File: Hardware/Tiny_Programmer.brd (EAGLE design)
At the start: 59.7 x 15.2 mm, 31 parts, among them Q1 16MHz, U1 ATTINY84, X1 USB-A-H

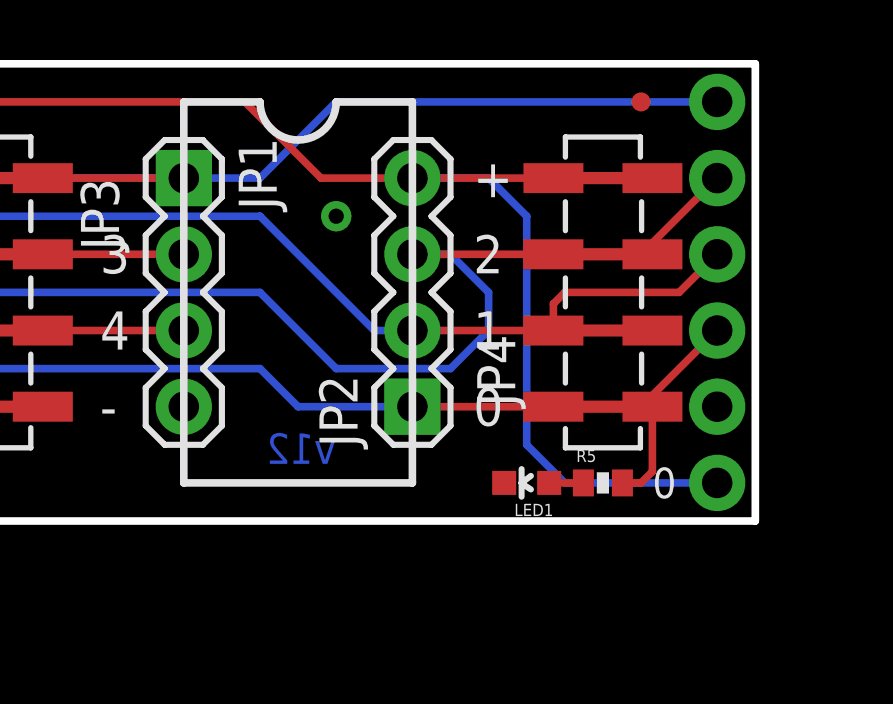
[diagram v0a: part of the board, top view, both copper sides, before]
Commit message: Modifies the new 6-pin SIP to be more compatible with an FTDI.
The new pin out should allow MOSI and MISO to bit-bang serial and
communicate over an FTDI connection for serial debuggin.
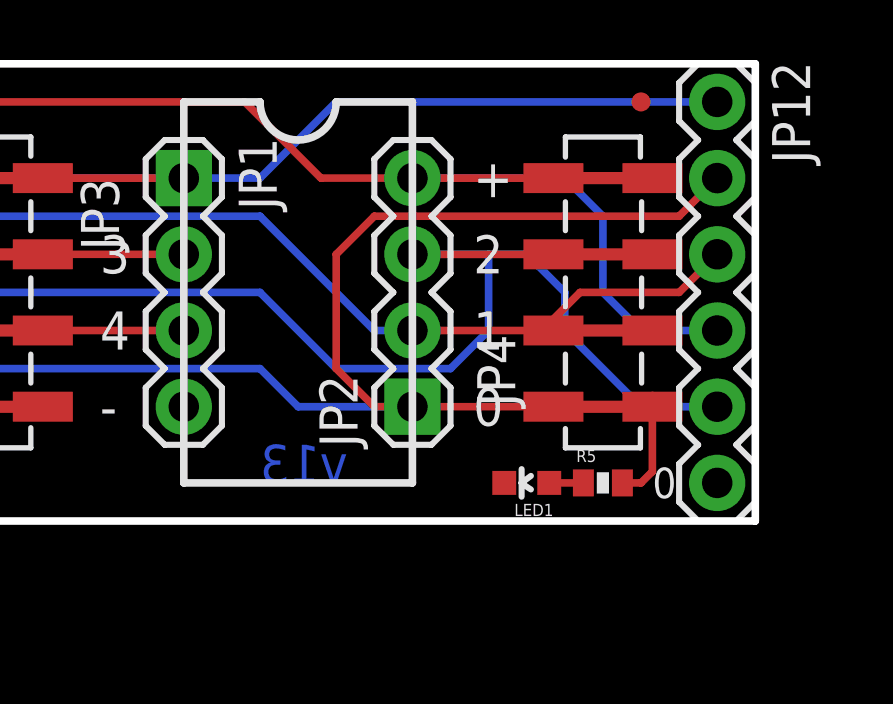
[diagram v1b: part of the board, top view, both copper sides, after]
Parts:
- flipped JP12 to the top
- renumbered JP10 to JP12
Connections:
- net GND: now also JP12.6; no longer JP12.5
- net MOSI: now also JP12.2; no longer JP12.4
- net SCK: now also JP12.5; no longer JP12.2
- net VCC: now also JP12.4; no longer JP12.6
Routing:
- net MOSI: track 64.9 -> 82.5 mm
- net SCK: track 58.0 -> 65.8 mm
- net VCC: track 86.5 -> 81.5 mm
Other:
- board text added: "GND"
- board text added: "v13"
- board text removed: "v12"
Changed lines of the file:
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@@
 <?xml version="1.0" encoding="utf-8"?>
 <!DOCTYPE eagle SYSTEM "eagle.dtd">
-<eagle version="6.4">
+<eagle version="6.5.0">
 <drawing>
 <settings>
@@
 <layer number="106" name="bPlate" color="7" fill="1" visible="no" active="yes"/>
 <layer number="107" name="Crop" color="7" fill="1" visible="no" active="yes"/>
+<layer number="108" name="tplace-old" color="10" fill="1" visible="yes" active="yes"/>
+<layer number="109" name="ref-old" color="11" fill="1" visible="yes" active="yes"/>
 <layer number="116" name="Patch_BOT" color="9" fill="4" visible="no" active="yes"/>
 <layer number="121" name="_tsilk" color="7" fill="1" visible="no" active="yes"/>
@@
 <wire x1="43.18" y1="13.97" x2="45.72" y2="13.97" width="0.254" layer="21" curve="180"/>
 <text x="38.1" y="1.27" size="1.778" layer="22" font="vector" ratio="15" rot="MR0">Tiny Programmer</text>
-<text x="45.72" y="1.905" size="1.016" layer="16" font="vector" ratio="20" rot="MR0">v12</text>
+<text x="46.101" y="1.27" size="1.27" layer="16" font="vector" ratio="20" rot="MR0">v13</text>
 <text x="1.27" y="-12.7" size="1.778" layer="27" font="vector" ratio="15">David A. Mellis, Jordan McConnell</text>
 <text x="23.241" y="13.97" size="0.8128" layer="21" font="vector" ratio="15" rot="SR0">RST</text>
@@
 <wire x1="0.889" y1="2.159" x2="1.016" y2="2.286" width="0.254" layer="49"/>
 <text x="55.499" y="6.731" size="0.8128" layer="22" font="vector" ratio="15" rot="SMR90">ISP</text>
-<text x="55.88" y="0.254" size="0.8128" layer="22" font="vector" ratio="15" rot="SMR90">VCC</text>
+<text x="55.88" y="0.254" size="0.8128" layer="22" font="vector" ratio="15" rot="SMR90">GND</text>
 <text x="55.88" y="12.954" size="0.8128" layer="22" font="vector" ratio="15" rot="SMR90">RST</text>
 <wire x1="55.88" y1="8.89" x2="55.88" y2="12.192" width="0.254" layer="22"/>
@@
 <element name="JP7" library="SparkFun" package="MICRO-FIDUCIAL" value="FIDUCIALUFIDUCIAL" x="6.35" y="1.27"/>
 <element name="JP8" library="SparkFun" package="MICRO-FIDUCIAL" value="FIDUCIALUFIDUCIAL" x="55.88" y="13.97"/>
-<element name="JP10" library="SparkFun-Connectors" package="1X06" value="" x="58.42" y="13.97" rot="MR270"/>
 <element name="JP11" library="SparkFun-Aesthetics" package="SFE-LOGO-FLAME" value="LOGO-SFESK" x="9.906" y="8.636" rot="MR90"/>
+<element name="JP12" library="SparkFun-Connectors" package="1X06" value="" x="58.42" y="13.97" rot="R270"/>
 </elements>
 <signals>
@@
 <wire x1="7.62" y1="4.46" x2="6.365" y2="4.46" width="0.254" layer="1"/>
 <wire x1="28.7981" y1="13.8121" x2="28.956" y2="13.97" width="0.254" layer="1"/>
-<contactref element="JP10" pad="6"/>
-<wire x1="58.42" y1="1.27" x2="53.34" y2="1.27" width="0.254" layer="16"/>
-<wire x1="53.34" y1="1.27" x2="52.07" y2="2.54" width="0.254" layer="16"/>
-<wire x1="52.07" y1="2.54" x2="52.07" y2="10.16" width="0.254" layer="16"/>
-<wire x1="52.07" y1="10.16" x2="50.8" y2="11.43" width="0.254" layer="16"/>
-<wire x1="50.8" y1="11.43" x2="48.26" y2="11.43" width="0.254" layer="16"/>
 <wire x1="18.04" y1="3.81" x2="19.05" y2="3.81" width="0.254" layer="1"/>
 <wire x1="19.05" y1="3.81" x2="20.32" y2="2.54" width="0.254" layer="1"/>
@@
 <wire x1="29.21" y1="2.54" x2="30.48" y2="3.81" width="0.254" layer="1"/>
 <wire x1="30.48" y1="3.81" x2="30.48" y2="13.97" width="0.254" layer="1"/>
+<contactref element="JP12" pad="4"/>
+<wire x1="58.42" y1="6.35" x2="55.88" y2="6.35" width="0.254" layer="16"/>
+<wire x1="55.88" y1="6.35" x2="54.61" y2="7.62" width="0.254" layer="16"/>
+<wire x1="54.61" y1="7.62" x2="54.61" y2="10.16" width="0.254" layer="16"/>
+<wire x1="54.61" y1="10.16" x2="53.34" y2="11.43" width="0.254" layer="16"/>
+<wire x1="53.34" y1="11.43" x2="48.26" y2="11.43" width="0.254" layer="16"/>
 </signal>
 <signal name="GND">
@@
 <contactref element="C2" pad="2"/>
 <contactref element="JP9" pad="6"/>
-<contactref element="JP10" pad="5"/>
-<via x="45.72" y="10.16" extent="1-16" drill="0.508"/>
 <via x="21.59" y="12.7" extent="1-16" drill="0.508"/>
+<contactref element="JP12" pad="6"/>
 </signal>
 <signal name="MOSI">
@@
 <wire x1="26.67" y1="3.81" x2="26.67" y2="6.35" width="0.254" layer="16"/>
 <wire x1="26.67" y1="6.35" x2="27.94" y2="7.62" width="0.254" layer="16"/>
-<contactref element="JP10" pad="4"/>
 <wire x1="56.26" y1="3.81" x2="56.26" y2="4.19" width="0.254" layer="1"/>
-<wire x1="56.26" y1="4.19" x2="58.42" y2="6.35" width="0.254" layer="1"/>
 <wire x1="48.26" y1="3.81" x2="44.45" y2="3.81" width="0.254" layer="16"/>
 <wire x1="44.45" y1="3.81" x2="43.18" y2="5.08" width="0.254" layer="16"/>
 <wire x1="43.18" y1="5.08" x2="30.48" y2="5.08" width="0.254" layer="16"/>
 <wire x1="30.48" y1="5.08" x2="27.94" y2="7.62" width="0.254" layer="16"/>
+<contactref element="JP12" pad="2"/>
+<wire x1="58.42" y1="11.43" x2="57.15" y2="10.16" width="0.254" layer="1"/>
+<wire x1="57.15" y1="10.16" x2="46.99" y2="10.16" width="0.254" layer="1"/>
+<wire x1="46.99" y1="10.16" x2="45.72" y2="8.89" width="0.254" layer="1"/>
+<wire x1="45.72" y1="8.89" x2="45.72" y2="5.08" width="0.254" layer="1"/>
+<wire x1="45.72" y1="5.08" x2="46.99" y2="3.81" width="0.254" layer="1"/>
+<wire x1="46.99" y1="3.81" x2="48.26" y2="3.81" width="0.254" layer="1"/>
 </signal>
 <signal name="MISO">
@@
 <wire x1="29.21" y1="11.43" x2="30.48" y2="10.16" width="0.254" layer="16"/>
 <wire x1="30.48" y1="10.16" x2="43.18" y2="10.16" width="0.254" layer="16"/>
-<contactref element="JP10" pad="3"/>
 <wire x1="43.18" y1="10.16" x2="46.99" y2="6.35" width="0.254" layer="16"/>
 <wire x1="46.99" y1="6.35" x2="48.26" y2="6.35" width="0.254" layer="16"/>
-<wire x1="52.96" y1="6.35" x2="52.96" y2="7.24" width="0.254" layer="1"/>
-<wire x1="52.96" y1="7.24" x2="53.34" y2="7.62" width="0.254" layer="1"/>
-<wire x1="53.34" y1="7.62" x2="57.15" y2="7.62" width="0.254" layer="1"/>
-<wire x1="57.15" y1="7.62" x2="58.42" y2="8.89" width="0.254" layer="1"/>
+<contactref element="JP12" pad="3"/>
+<wire x1="58.42" y1="8.89" x2="57.15" y2="7.62" width="0.254" layer="1"/>
+<wire x1="52.96" y1="6.35" x2="52.96" y2="6.732" width="0.254" layer="1"/>
+<wire x1="52.96" y1="6.732" x2="53.848" y2="7.62" width="0.254" layer="1"/>
+<wire x1="53.848" y1="7.62" x2="57.15" y2="7.62" width="0.254" layer="1"/>
 </signal>
 <signal name="SCK">
@@
 <wire x1="43.18" y1="7.62" x2="30.48" y2="7.62" width="0.254" layer="16"/>
 <wire x1="30.48" y1="7.62" x2="29.21" y2="8.89" width="0.254" layer="16"/>
-<contactref element="JP10" pad="2"/>
 <wire x1="43.18" y1="7.62" x2="45.72" y2="5.08" width="0.254" layer="16"/>
 <wire x1="45.72" y1="5.08" x2="49.53" y2="5.08" width="0.254" layer="16"/>
 <wire x1="49.53" y1="5.08" x2="50.8" y2="6.35" width="0.254" layer="16"/>
-<wire x1="50.8" y1="6.35" x2="50.8" y2="7.62" width="0.254" layer="16"/>
-<wire x1="50.8" y1="7.62" x2="49.53" y2="8.89" width="0.254" layer="16"/>
-<wire x1="56.26" y1="8.89" x2="56.26" y2="9.27" width="0.254" layer="1"/>
-<wire x1="56.26" y1="9.27" x2="58.42" y2="11.43" width="0.254" layer="1"/>
-<wire x1="48.26" y1="8.89" x2="49.53" y2="8.89" width="0.254" layer="16"/>
 <wire x1="56.26" y1="8.89" x2="48.26" y2="8.89" width="0.254" layer="1"/>
+<contactref element="JP12" pad="5"/>
+<wire x1="58.42" y1="3.81" x2="55.88" y2="3.81" width="0.254" layer="16"/>
+<wire x1="55.88" y1="3.81" x2="53.34" y2="6.35" width="0.254" layer="16"/>
+<wire x1="53.34" y1="6.35" x2="53.34" y2="7.62" width="0.254" layer="16"/>
+<wire x1="53.34" y1="7.62" x2="52.07" y2="8.89" width="0.254" layer="16"/>
+<wire x1="52.07" y1="8.89" x2="50.8" y2="8.89" width="0.254" layer="16"/>
+<wire x1="50.8" y1="8.89" x2="48.26" y2="8.89" width="0.254" layer="16"/>
+<wire x1="50.8" y1="6.35" x2="50.8" y2="8.89" width="0.254" layer="16"/>
 </signal>
 <signal name="RST">
@@
 <via x="26.67" y="12.7" extent="1-16" drill="0.508"/>
 <wire x1="26.67" y1="12.7" x2="24.58" y2="12.7" width="0.254" layer="1"/>
-<contactref element="JP10" pad="1"/>
-<wire x1="58.42" y1="13.97" x2="45.72" y2="13.97" width="0.254" layer="16"/>
-<wire x1="45.72" y1="13.97" x2="43.18" y2="11.43" width="0.254" layer="16"/>
-<wire x1="43.18" y1="11.43" x2="40.64" y2="11.43" width="0.254" layer="16"/>
+<contactref element="JP12" pad="1"/>
+<wire x1="40.64" y1="11.43" x2="43.18" y2="11.43" width="0.254" layer="16"/>
+<wire x1="43.18" y1="11.43" x2="45.72" y2="13.97" width="0.254" layer="16"/>
+<wire x1="45.72" y1="13.97" x2="58.42" y2="13.97" width="0.254" layer="16"/>
 </signal>
 <signal name="D-">

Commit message: Revert "Modifies the new 6-pin SIP to be more compatible with an FTDI."
This reverts commit e9ce5eee6c851359ce4a9d7fdec24ce809564be4.
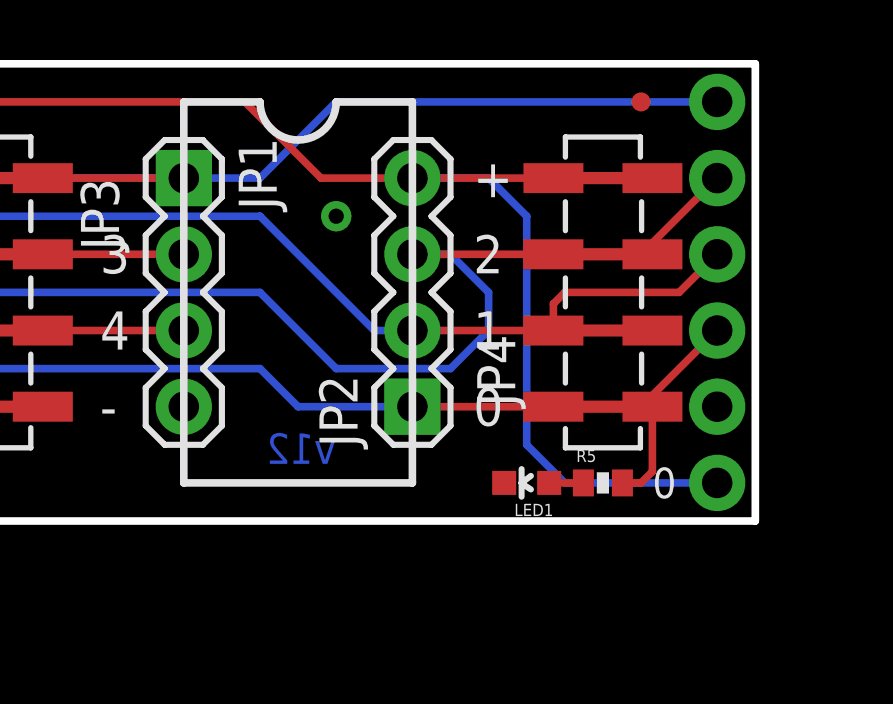
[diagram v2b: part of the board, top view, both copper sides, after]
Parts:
- flipped JP10 to the bottom
- renumbered JP12 to JP10
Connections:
- net GND: now also JP10.5; no longer JP10.6
- net MOSI: now also JP10.4; no longer JP10.2
- net SCK: now also JP10.2; no longer JP10.5
- net VCC: now also JP10.6; no longer JP10.4
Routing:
- net MOSI: track 82.5 -> 64.9 mm
- net SCK: track 65.8 -> 58.0 mm
- net VCC: track 81.5 -> 86.5 mm
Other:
- board text added: "v12"
- board text removed: "GND"
- board text removed: "v13"
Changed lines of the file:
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@@
 <?xml version="1.0" encoding="utf-8"?>
 <!DOCTYPE eagle SYSTEM "eagle.dtd">
-<eagle version="6.5.0">
+<eagle version="6.4">
 <drawing>
 <settings>
@@
 <layer number="106" name="bPlate" color="7" fill="1" visible="no" active="yes"/>
 <layer number="107" name="Crop" color="7" fill="1" visible="no" active="yes"/>
-<layer number="108" name="tplace-old" color="10" fill="1" visible="yes" active="yes"/>
-<layer number="109" name="ref-old" color="11" fill="1" visible="yes" active="yes"/>
 <layer number="116" name="Patch_BOT" color="9" fill="4" visible="no" active="yes"/>
 <layer number="121" name="_tsilk" color="7" fill="1" visible="no" active="yes"/>
@@
 <wire x1="43.18" y1="13.97" x2="45.72" y2="13.97" width="0.254" layer="21" curve="180"/>
 <text x="38.1" y="1.27" size="1.778" layer="22" font="vector" ratio="15" rot="MR0">Tiny Programmer</text>
-<text x="46.101" y="1.27" size="1.27" layer="16" font="vector" ratio="20" rot="MR0">v13</text>
+<text x="45.72" y="1.905" size="1.016" layer="16" font="vector" ratio="20" rot="MR0">v12</text>
 <text x="1.27" y="-12.7" size="1.778" layer="27" font="vector" ratio="15">David A. Mellis, Jordan McConnell</text>
 <text x="23.241" y="13.97" size="0.8128" layer="21" font="vector" ratio="15" rot="SR0">RST</text>
@@
 <wire x1="0.889" y1="2.159" x2="1.016" y2="2.286" width="0.254" layer="49"/>
 <text x="55.499" y="6.731" size="0.8128" layer="22" font="vector" ratio="15" rot="SMR90">ISP</text>
-<text x="55.88" y="0.254" size="0.8128" layer="22" font="vector" ratio="15" rot="SMR90">GND</text>
+<text x="55.88" y="0.254" size="0.8128" layer="22" font="vector" ratio="15" rot="SMR90">VCC</text>
 <text x="55.88" y="12.954" size="0.8128" layer="22" font="vector" ratio="15" rot="SMR90">RST</text>
 <wire x1="55.88" y1="8.89" x2="55.88" y2="12.192" width="0.254" layer="22"/>
@@
 <element name="JP7" library="SparkFun" package="MICRO-FIDUCIAL" value="FIDUCIALUFIDUCIAL" x="6.35" y="1.27"/>
 <element name="JP8" library="SparkFun" package="MICRO-FIDUCIAL" value="FIDUCIALUFIDUCIAL" x="55.88" y="13.97"/>
+<element name="JP10" library="SparkFun-Connectors" package="1X06" value="" x="58.42" y="13.97" rot="MR270"/>
 <element name="JP11" library="SparkFun-Aesthetics" package="SFE-LOGO-FLAME" value="LOGO-SFESK" x="9.906" y="8.636" rot="MR90"/>
-<element name="JP12" library="SparkFun-Connectors" package="1X06" value="" x="58.42" y="13.97" rot="R270"/>
 </elements>
 <signals>
@@
 <wire x1="7.62" y1="4.46" x2="6.365" y2="4.46" width="0.254" layer="1"/>
 <wire x1="28.7981" y1="13.8121" x2="28.956" y2="13.97" width="0.254" layer="1"/>
+<contactref element="JP10" pad="6"/>
+<wire x1="58.42" y1="1.27" x2="53.34" y2="1.27" width="0.254" layer="16"/>
+<wire x1="53.34" y1="1.27" x2="52.07" y2="2.54" width="0.254" layer="16"/>
+<wire x1="52.07" y1="2.54" x2="52.07" y2="10.16" width="0.254" layer="16"/>
+<wire x1="52.07" y1="10.16" x2="50.8" y2="11.43" width="0.254" layer="16"/>
+<wire x1="50.8" y1="11.43" x2="48.26" y2="11.43" width="0.254" layer="16"/>
 <wire x1="18.04" y1="3.81" x2="19.05" y2="3.81" width="0.254" layer="1"/>
 <wire x1="19.05" y1="3.81" x2="20.32" y2="2.54" width="0.254" layer="1"/>
@@
 <wire x1="29.21" y1="2.54" x2="30.48" y2="3.81" width="0.254" layer="1"/>
 <wire x1="30.48" y1="3.81" x2="30.48" y2="13.97" width="0.254" layer="1"/>
-<contactref element="JP12" pad="4"/>
-<wire x1="58.42" y1="6.35" x2="55.88" y2="6.35" width="0.254" layer="16"/>
-<wire x1="55.88" y1="6.35" x2="54.61" y2="7.62" width="0.254" layer="16"/>
-<wire x1="54.61" y1="7.62" x2="54.61" y2="10.16" width="0.254" layer="16"/>
-<wire x1="54.61" y1="10.16" x2="53.34" y2="11.43" width="0.254" layer="16"/>
-<wire x1="53.34" y1="11.43" x2="48.26" y2="11.43" width="0.254" layer="16"/>
 </signal>
 <signal name="GND">
@@
 <contactref element="C2" pad="2"/>
 <contactref element="JP9" pad="6"/>
+<contactref element="JP10" pad="5"/>
+<via x="45.72" y="10.16" extent="1-16" drill="0.508"/>
 <via x="21.59" y="12.7" extent="1-16" drill="0.508"/>
-<contactref element="JP12" pad="6"/>
 </signal>
 <signal name="MOSI">
@@
 <wire x1="26.67" y1="3.81" x2="26.67" y2="6.35" width="0.254" layer="16"/>
 <wire x1="26.67" y1="6.35" x2="27.94" y2="7.62" width="0.254" layer="16"/>
+<contactref element="JP10" pad="4"/>
 <wire x1="56.26" y1="3.81" x2="56.26" y2="4.19" width="0.254" layer="1"/>
+<wire x1="56.26" y1="4.19" x2="58.42" y2="6.35" width="0.254" layer="1"/>
 <wire x1="48.26" y1="3.81" x2="44.45" y2="3.81" width="0.254" layer="16"/>
 <wire x1="44.45" y1="3.81" x2="43.18" y2="5.08" width="0.254" layer="16"/>
 <wire x1="43.18" y1="5.08" x2="30.48" y2="5.08" width="0.254" layer="16"/>
 <wire x1="30.48" y1="5.08" x2="27.94" y2="7.62" width="0.254" layer="16"/>
-<contactref element="JP12" pad="2"/>
-<wire x1="58.42" y1="11.43" x2="57.15" y2="10.16" width="0.254" layer="1"/>
-<wire x1="57.15" y1="10.16" x2="46.99" y2="10.16" width="0.254" layer="1"/>
-<wire x1="46.99" y1="10.16" x2="45.72" y2="8.89" width="0.254" layer="1"/>
-<wire x1="45.72" y1="8.89" x2="45.72" y2="5.08" width="0.254" layer="1"/>
-<wire x1="45.72" y1="5.08" x2="46.99" y2="3.81" width="0.254" layer="1"/>
-<wire x1="46.99" y1="3.81" x2="48.26" y2="3.81" width="0.254" layer="1"/>
 </signal>
 <signal name="MISO">
@@
 <wire x1="29.21" y1="11.43" x2="30.48" y2="10.16" width="0.254" layer="16"/>
 <wire x1="30.48" y1="10.16" x2="43.18" y2="10.16" width="0.254" layer="16"/>
+<contactref element="JP10" pad="3"/>
 <wire x1="43.18" y1="10.16" x2="46.99" y2="6.35" width="0.254" layer="16"/>
 <wire x1="46.99" y1="6.35" x2="48.26" y2="6.35" width="0.254" layer="16"/>
-<contactref element="JP12" pad="3"/>
-<wire x1="58.42" y1="8.89" x2="57.15" y2="7.62" width="0.254" layer="1"/>
-<wire x1="52.96" y1="6.35" x2="52.96" y2="6.732" width="0.254" layer="1"/>
-<wire x1="52.96" y1="6.732" x2="53.848" y2="7.62" width="0.254" layer="1"/>
-<wire x1="53.848" y1="7.62" x2="57.15" y2="7.62" width="0.254" layer="1"/>
+<wire x1="52.96" y1="6.35" x2="52.96" y2="7.24" width="0.254" layer="1"/>
+<wire x1="52.96" y1="7.24" x2="53.34" y2="7.62" width="0.254" layer="1"/>
+<wire x1="53.34" y1="7.62" x2="57.15" y2="7.62" width="0.254" layer="1"/>
+<wire x1="57.15" y1="7.62" x2="58.42" y2="8.89" width="0.254" layer="1"/>
 </signal>
 <signal name="SCK">
@@
 <wire x1="43.18" y1="7.62" x2="30.48" y2="7.62" width="0.254" layer="16"/>
 <wire x1="30.48" y1="7.62" x2="29.21" y2="8.89" width="0.254" layer="16"/>
+<contactref element="JP10" pad="2"/>
 <wire x1="43.18" y1="7.62" x2="45.72" y2="5.08" width="0.254" layer="16"/>
 <wire x1="45.72" y1="5.08" x2="49.53" y2="5.08" width="0.254" layer="16"/>
 <wire x1="49.53" y1="5.08" x2="50.8" y2="6.35" width="0.254" layer="16"/>
+<wire x1="50.8" y1="6.35" x2="50.8" y2="7.62" width="0.254" layer="16"/>
+<wire x1="50.8" y1="7.62" x2="49.53" y2="8.89" width="0.254" layer="16"/>
+<wire x1="56.26" y1="8.89" x2="56.26" y2="9.27" width="0.254" layer="1"/>
+<wire x1="56.26" y1="9.27" x2="58.42" y2="11.43" width="0.254" layer="1"/>
+<wire x1="48.26" y1="8.89" x2="49.53" y2="8.89" width="0.254" layer="16"/>
 <wire x1="56.26" y1="8.89" x2="48.26" y2="8.89" width="0.254" layer="1"/>
-<contactref element="JP12" pad="5"/>
-<wire x1="58.42" y1="3.81" x2="55.88" y2="3.81" width="0.254" layer="16"/>
-<wire x1="55.88" y1="3.81" x2="53.34" y2="6.35" width="0.254" layer="16"/>
-<wire x1="53.34" y1="6.35" x2="53.34" y2="7.62" width="0.254" layer="16"/>
-<wire x1="53.34" y1="7.62" x2="52.07" y2="8.89" width="0.254" layer="16"/>
-<wire x1="52.07" y1="8.89" x2="50.8" y2="8.89" width="0.254" layer="16"/>
-<wire x1="50.8" y1="8.89" x2="48.26" y2="8.89" width="0.254" layer="16"/>
-<wire x1="50.8" y1="6.35" x2="50.8" y2="8.89" width="0.254" layer="16"/>
 </signal>
 <signal name="RST">
@@
 <via x="26.67" y="12.7" extent="1-16" drill="0.508"/>
 <wire x1="26.67" y1="12.7" x2="24.58" y2="12.7" width="0.254" layer="1"/>
-<contactref element="JP12" pad="1"/>
-<wire x1="40.64" y1="11.43" x2="43.18" y2="11.43" width="0.254" layer="16"/>
-<wire x1="43.18" y1="11.43" x2="45.72" y2="13.97" width="0.254" layer="16"/>
-<wire x1="45.72" y1="13.97" x2="58.42" y2="13.97" width="0.254" layer="16"/>
+<contactref element="JP10" pad="1"/>
+<wire x1="58.42" y1="13.97" x2="45.72" y2="13.97" width="0.254" layer="16"/>
+<wire x1="45.72" y1="13.97" x2="43.18" y2="11.43" width="0.254" layer="16"/>
+<wire x1="43.18" y1="11.43" x2="40.64" y2="11.43" width="0.254" layer="16"/>
 </signal>
 <signal name="D-">
